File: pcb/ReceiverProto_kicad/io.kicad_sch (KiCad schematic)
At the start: 7 parts, among them J1 Conn_01x09, J2 Conn_01x03, J3 Conn_01x04, J4 Conn_01x06

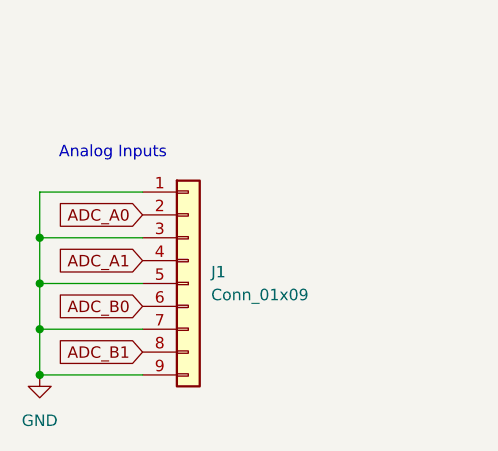
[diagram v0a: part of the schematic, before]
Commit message: add 5V filtering cap, reordered analog input pins
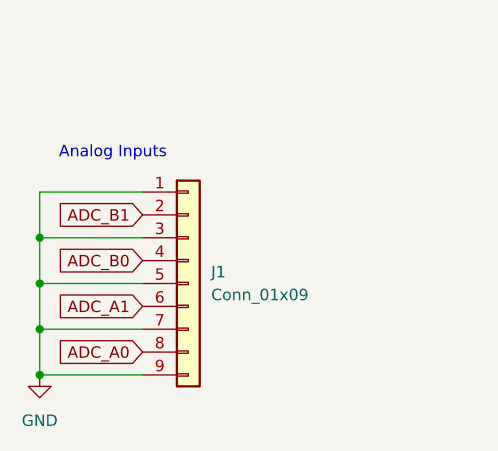
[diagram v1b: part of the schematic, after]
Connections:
- net ADC_A0: now also J1.8 (Pin_8); no longer J1.2 (Pin_2)
- net ADC_A1: now also J1.6 (Pin_6); no longer J1.4 (Pin_4)
- net ADC_B0: now also J1.4 (Pin_4); no longer J1.6 (Pin_6)
- net ADC_B1: now also J1.2 (Pin_2); no longer J1.8 (Pin_8)
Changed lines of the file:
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@@
 	(global_label "ADC_B0"
 		(shape input)
-		(at 81.28 113.03 180)
+		(at 81.28 107.95 180)
 		(fields_autoplaced yes)
 		(effects
@@
 		)
 		(property "Intersheetrefs" "${INTERSHEET_REFS}"
-			(at 71.2191 113.03 0)
+			(at 71.2191 107.95 0)
 			(effects
 				(font
@@
 	(global_label "ADC_A1"
 		(shape input)
-		(at 81.28 107.95 180)
+		(at 81.28 113.03 180)
 		(fields_autoplaced yes)
 		(effects
@@
 		)
 		(property "Intersheetrefs" "${INTERSHEET_REFS}"
-			(at 71.4005 107.95 0)
+			(at 71.4005 113.03 0)
 			(effects
 				(font
@@
 	(global_label "ADC_B1"
 		(shape input)
-		(at 81.28 118.11 180)
+		(at 81.28 102.87 180)
 		(fields_autoplaced yes)
 		(effects
@@
 		)
 		(property "Intersheetrefs" "${INTERSHEET_REFS}"
-			(at 71.2191 118.11 0)
+			(at 71.2191 102.87 0)
 			(effects
 				(font
@@
 	(global_label "ADC_A0"
 		(shape input)
-		(at 81.28 102.87 180)
+		(at 81.28 118.11 180)
 		(fields_autoplaced yes)
 		(effects
@@
 		)
 		(property "Intersheetrefs" "${INTERSHEET_REFS}"
-			(at 71.4005 102.87 0)
+			(at 71.4005 118.11 0)
 			(effects
 				(font

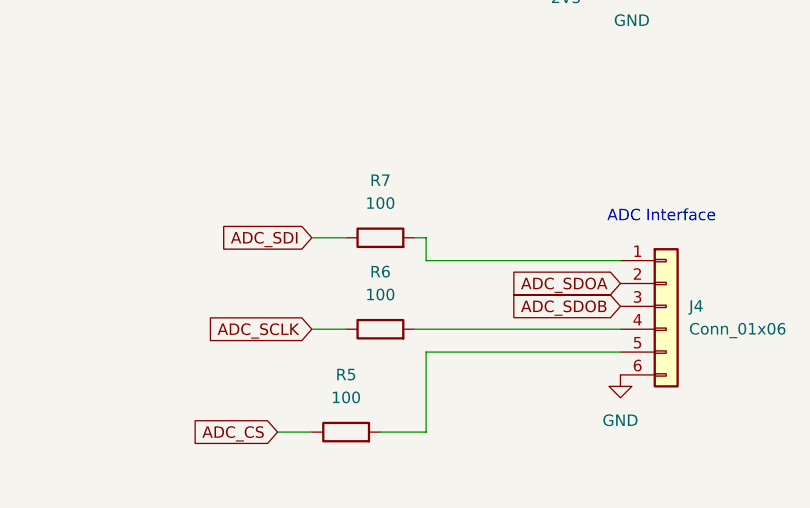
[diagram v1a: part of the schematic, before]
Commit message: major progress on board layout, slight schematic tweaks for ease of routing
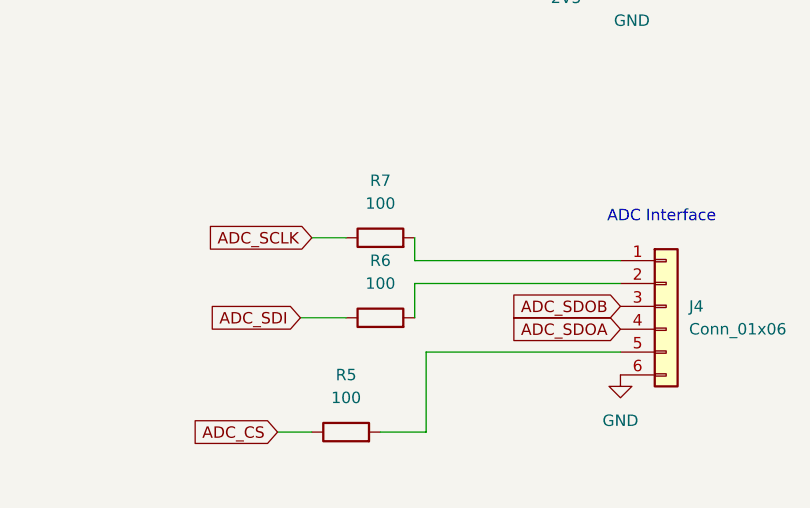
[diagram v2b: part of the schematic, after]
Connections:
- net ADC_SCLK: now also R7.1; no longer R6.1
- net ADC_SDI: now also R6.1; no longer R7.1
- net ADC_SDOA: now also J4.4 (Pin_4); no longer J4.2 (Pin_2)
- net at R6.2: now also J4.2 (Pin_2); no longer J4.4 (Pin_4)
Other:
- moved on the sheet: R6
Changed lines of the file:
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@@
 	(wire
 		(pts
-			(xy 222.25 101.6) (xy 243.84 101.6)
+			(xy 220.98 99.06) (xy 220.98 101.6)
 		)
 		(stroke
@@
 	(wire
 		(pts
+			(xy 220.98 107.95) (xy 220.98 104.14)
+		)
+		(stroke
+			(width 0)
+			(type default)
+		)
+	)
+	(wire
+		(pts
 			(xy 69.85 105.41) (xy 69.85 110.49)
 		)
@@
 	(wire
 		(pts
-			(xy 209.55 109.22) (xy 213.36 109.22)
-		)
-		(stroke
-			(width 0)
-			(type default)
-		)
-	)
-	(wire
-		(pts
 			(xy 217.17 120.65) (xy 222.25 120.65)
 		)
@@
 	(wire
 		(pts
-			(xy 220.98 99.06) (xy 222.25 99.06)
+			(xy 208.28 107.95) (xy 213.36 107.95)
+		)
+		(stroke
+			(width 0)
+			(type default)
+		)
+	)
+	(wire
+		(pts
+			(xy 220.98 101.6) (xy 243.84 101.6)
 		)
 		(stroke
@@
 	(wire
 		(pts
+			(xy 220.98 104.14) (xy 243.84 104.14)
+		)
+		(stroke
+			(width 0)
+			(type default)
+		)
+	)
+	(wire
+		(pts
 			(xy 209.55 99.06) (xy 213.36 99.06)
 		)
@@
 	(wire
 		(pts
-			(xy 220.98 109.22) (xy 243.84 109.22)
-		)
-		(stroke
-			(width 0)
-			(type default)
-		)
-	)
-	(wire
-		(pts
 			(xy 69.85 110.49) (xy 69.85 115.57)
 		)
@@
 		)
 	)
-	(wire
-		(pts
-			(xy 222.25 99.06) (xy 222.25 101.6)
-		)
-		(stroke
-			(width 0)
-			(type default)
-		)
-	)
 	(global_label "ADC_B0"
 		(shape input)
@@
 	(global_label "ADC_SDI"
 		(shape input)
+		(at 208.28 107.95 180)
+		(fields_autoplaced yes)
+		(effects
+			(font
+				(size 1.27 1.27)
+			)
+			(justify right)
+		)
+		(property "Intersheetrefs" "${INTERSHEET_REFS}"
+			(at 197.6143 107.95 0)
+			(effects
+				(font
+					(size 1.27 1.27)
+				)
+				(justify right)
+				(hide yes)
+			)
+		)
+	)
+	(global_label "VREF_DIV2"
+		(shape input)
+		(at 245.11 64.77 180)
+		(fields_autoplaced yes)
+		(effects
+			(font
+				(size 1.27 1.27)
+			)
+			(justify right)
+		)
+		(property "Intersheetrefs" "${INTERSHEET_REFS}"
+			(at 232.3881 64.77 0)
+			(effects
+				(font
+					(size 1.27 1.27)
+				)
+				(justify right)
+				(hide yes)
+			)
+		)
+	)
+	(global_label "ADC_CS"
+		(shape input)
+		(at 205.74 120.65 180)
+		(fields_autoplaced yes)
+		(effects
+			(font
+				(size 1.27 1.27)
+			)
+			(justify right)
+		)
+		(property "Intersheetrefs" "${INTERSHEET_REFS}"
+			(at 195.6791 120.65 0)
+			(effects
+				(font
+					(size 1.27 1.27)
+				)
+				(justify right)
+				(hide yes)
+			)
+		)
+	)
+	(global_label "ADC_SDOA"
+		(shape input)
+		(at 243.84 109.22 180)
+		(fields_autoplaced yes)
+		(effects
+			(font
+				(size 1.27 1.27)
+			)
+			(justify right)
+		)
+		(property "Intersheetrefs" "${INTERSHEET_REFS}"
+			(at 231.36 109.22 0)
+			(effects
+				(font
+					(size 1.27 1.27)
+				)
+				(justify right)
+				(hide yes)
+			)
+		)
+	)
+	(global_label "ADC_SCLK"
+		(shape input)
 		(at 209.55 99.06 180)
 		(fields_autoplaced yes)
@@
 		)
 		(property "Intersheetrefs" "${INTERSHEET_REFS}"
-			(at 198.8843 99.06 0)
-			(effects
-				(font
-					(size 1.27 1.27)
-				)
-				(justify right)
-				(hide yes)
-			)
-		)
-	)
-	(global_label "VREF_DIV2"
-		(shape input)
-		(at 245.11 64.77 180)
-		(fields_autoplaced yes)
-		(effects
-			(font
-				(size 1.27 1.27)
-			)
-			(justify right)
-		)
-		(property "Intersheetrefs" "${INTERSHEET_REFS}"
-			(at 232.3881 64.77 0)
-			(effects
-				(font
-					(size 1.27 1.27)
-				)
-				(justify right)
-				(hide yes)
-			)
-		)
-	)
-	(global_label "ADC_CS"
-		(shape input)
-		(at 205.74 120.65 180)
-		(fields_autoplaced yes)
-		(effects
-			(font
-				(size 1.27 1.27)
-			)
-			(justify right)
-		)
-		(property "Intersheetrefs" "${INTERSHEET_REFS}"
-			(at 195.6791 120.65 0)
-			(effects
-				(font
-					(size 1.27 1.27)
-				)
-				(justify right)
-				(hide yes)
-			)
-		)
-	)
-	(global_label "ADC_SDOA"
-		(shape input)
-		(at 243.84 104.14 180)
-		(fields_autoplaced yes)
-		(effects
-			(font
-				(size 1.27 1.27)
-			)
-			(justify right)
-		)
-		(property "Intersheetrefs" "${INTERSHEET_REFS}"
-			(at 231.36 104.14 0)
-			(effects
-				(font
-					(size 1.27 1.27)
-				)
-				(justify right)
-				(hide yes)
-			)
-		)
-	)
-	(global_label "ADC_SCLK"
-		(shape input)
-		(at 209.55 109.22 180)
-		(fields_autoplaced yes)
-		(effects
-			(font
-				(size 1.27 1.27)
-			)
-			(justify right)
-		)
-		(property "Intersheetrefs" "${INTERSHEET_REFS}"
-			(at 197.191 109.22 0)
+			(at 197.191 99.06 0)
 			(effects
 				(font
@@
 	(symbol
 		(lib_id "Device:R")
-		(at 217.17 109.22 90)
+		(at 217.17 107.95 90)
 		(unit 1)
 		(exclude_from_sim no)
@@
 		(fields_autoplaced yes)
 		(property "Reference" "R6"
-			(at 217.17 102.87 90)
+			(at 217.17 101.6 90)
 			(effects
 				(font
@@
 		)
 		(property "Value" "100"
-			(at 217.17 105.41 90)
+			(at 217.17 104.14 90)
 			(effects
 				(font
@@
 		)
 		(property "Footprint" "SMD_Passives:YAG_R0201_YAG_100"
-			(at 217.17 110.998 90)
+			(at 217.17 109.728 90)
 			(effects
 				(font
@@
 		)
 		(property "Datasheet" "~"
-			(at 217.17 109.22 0)
+			(at 217.17 107.95 0)
 			(effects
 				(font
@@
 		)
 		(property "Description" "Resistor"
-			(at 217.17 109.22 0)
-			(effects
-				(font
+			(at 217.17 107.95 0)
+			(effects
+				(font
